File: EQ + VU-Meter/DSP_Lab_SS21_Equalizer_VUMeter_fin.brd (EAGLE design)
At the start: 120 x 44 mm, 271 parts, among them IC1 TL072D, IC2 TL074D, IC3 TL074D, IC4 TL074D, IC5 TL072D, IC7 TL072D, J2 640455-4, T1 BC846A, T10 BC846A, T11 BC846A, T12 BC846A, T13 BC846A, T14 BC846A, T15 BC846A, T16 BC846A, T17 BC846A, T18 BC846A, T19 BC846A, T2 BC846A, T20 BC846A, T21 BC846A, T22 BC846A, T23 BC846A, T24 BC846A, T25 BC846A, T26 BC846A, T27 BC846A, T28 BC846A, T29 BC846A, T3 BC846A, T30 BC846A, T4 BC846A, T5 BC846A, T6 BC846A, T7 BC846A, T8 BC846A, T9 BC846A, U1 LM2611, U2 LMR62014

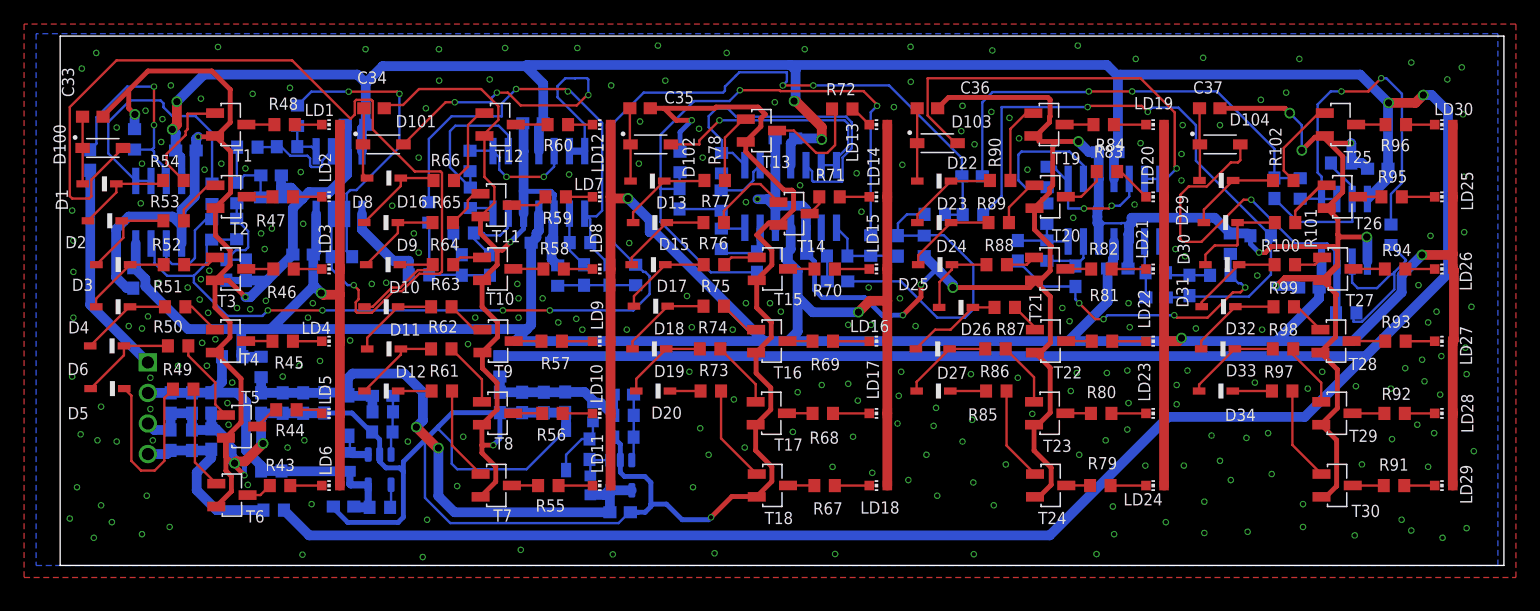
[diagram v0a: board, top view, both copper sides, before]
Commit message: Production data for ordering Mainboard, Keys, UI and EQ at JLCPCB
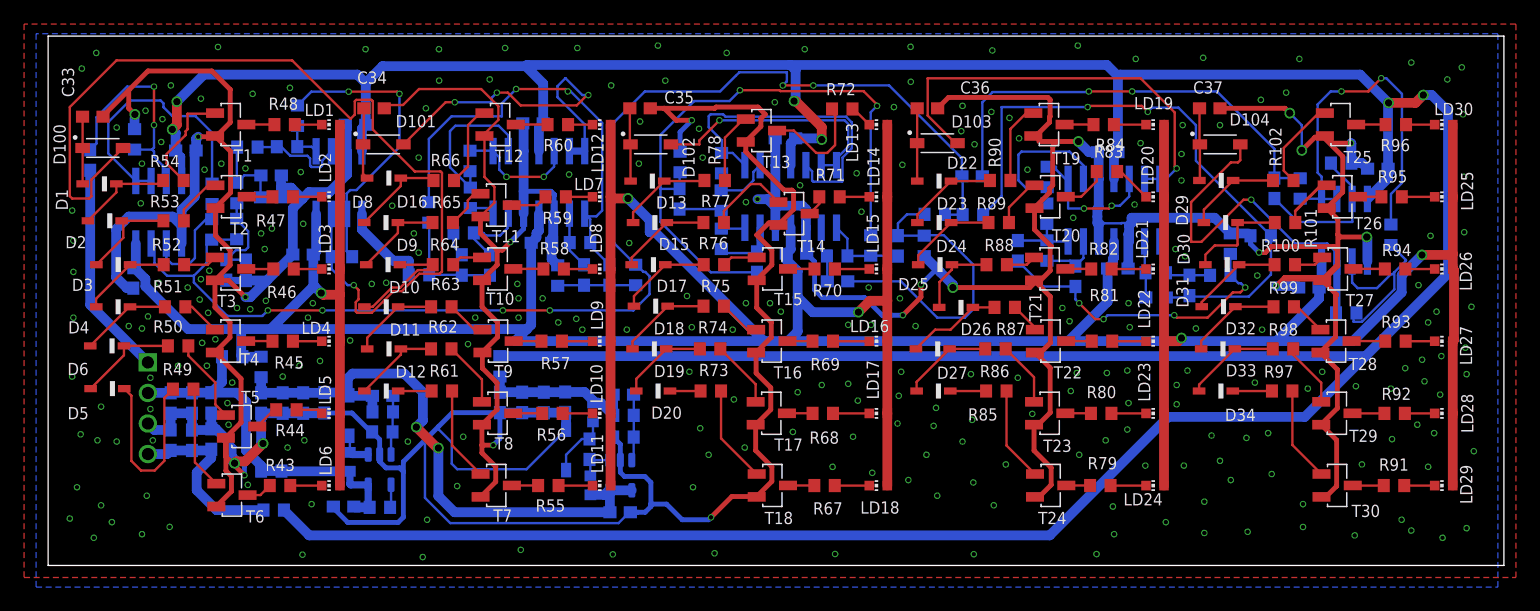
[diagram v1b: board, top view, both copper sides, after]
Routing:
- net HP_OUT: track 36.8 -> 34.7 mm
- net BP1_OUT: track 29.9 -> 29.2 mm
- net GND: vias 22 -> 278
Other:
- board size 120 x 44 mm -> 121 x 44 mm
